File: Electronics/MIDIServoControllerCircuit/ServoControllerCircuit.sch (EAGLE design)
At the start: 19 parts, among them IC1 MCP1700INLINE, J1 PJ-063BH, T1 2N3904, X1 SIGNAL-PWR-GND, X2 SIGNAL-PWR-GND

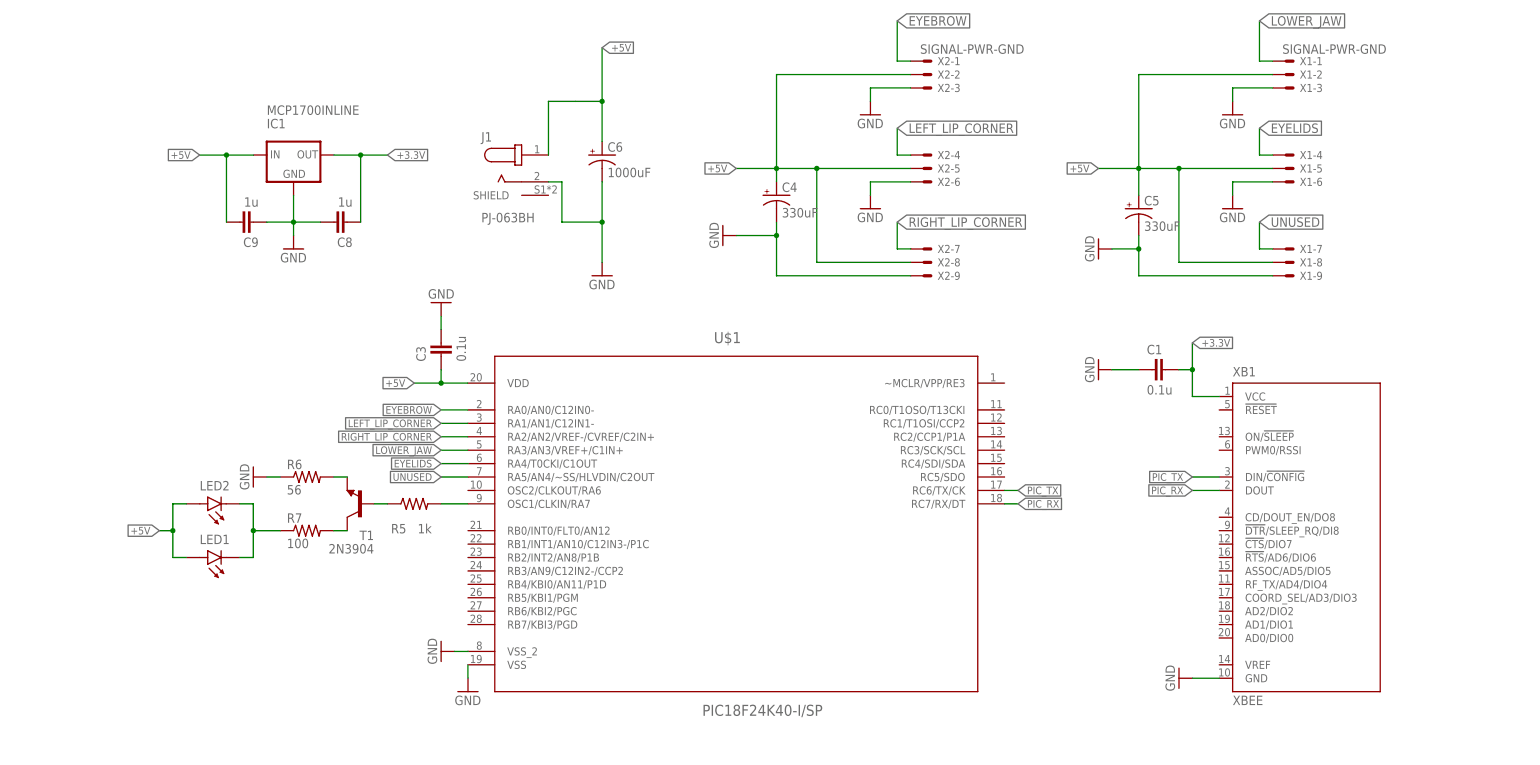
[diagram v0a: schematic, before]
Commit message: Reversing modifications made to Electronics that are ahread of the rest of the project.
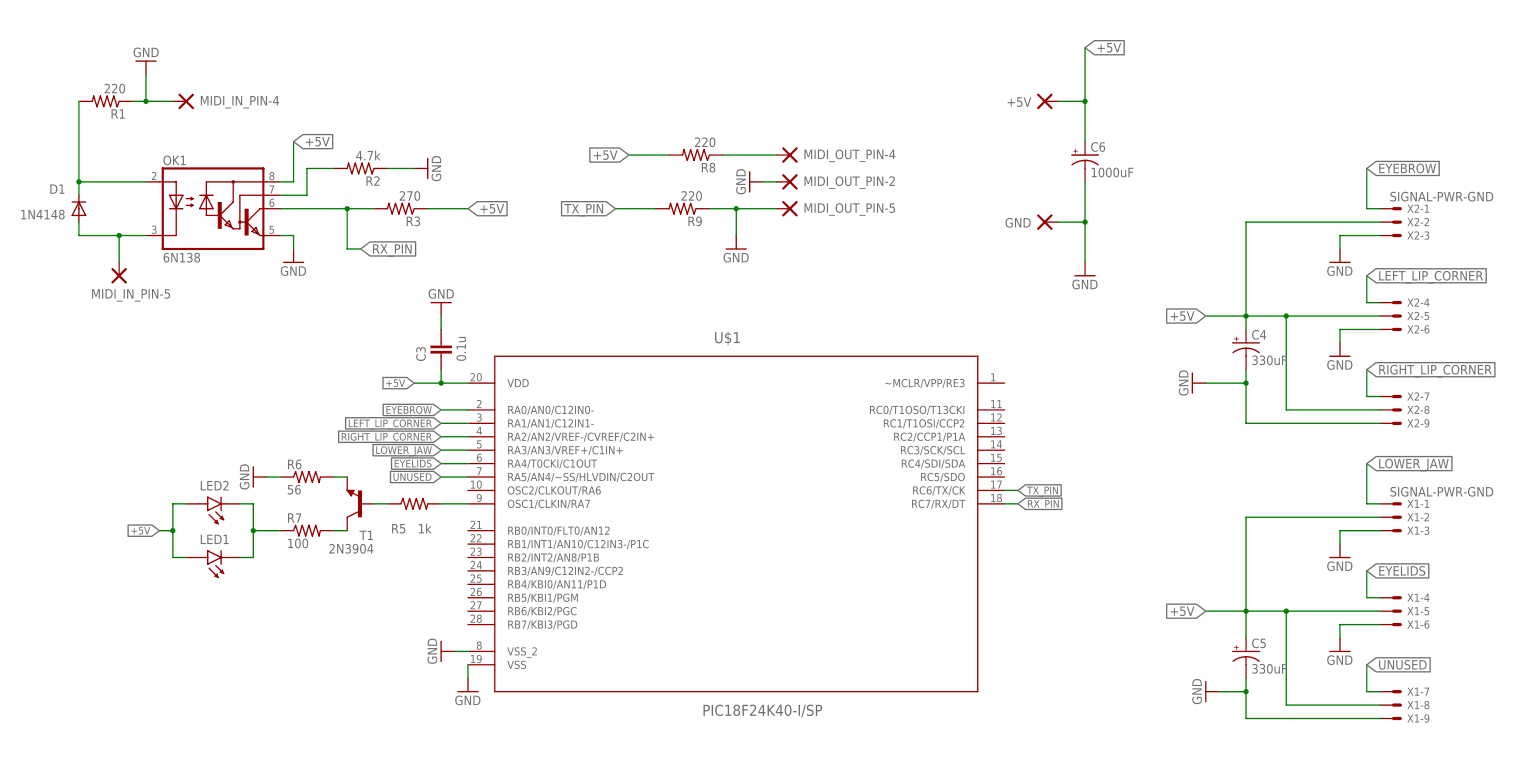
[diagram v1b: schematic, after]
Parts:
- removed C1: 0.1u, resistor:C-EU050-025X075
- removed C8, C9: 1u, resistor:C-EU050-025X075
- removed IC1: MCP1700INLINE, MCP1700:MCP1700INLINE
- removed J1: PJ-063BH, PJ-063BH:PJ-063BH
- removed XB1: XBEE, maxstream:XBEE
- added +5V, GND, MIDI_IN_PIN-4, MIDI_IN_PIN-5, MIDI_OUT_PIN-2, MIDI_OUT_PIN-4, MIDI_OUT_PIN-5: DOUBLE_THROUGH_HOLE_PAD, DOUBLE_THROUGH_HOLE_PAD:DOUBLE_THROUGH_HOLE_PAD
- added D1: 1N4148, diode:1N4148DO35-10
- added OK1: 6N138, optocoupler:6N138
- added R1, R8, R9: 220, resistor:R-US_0207/12
- added R2: 4.7k, resistor:R-US_0207/12
- added R3: 270, resistor:R-US_0207/12
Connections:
- removed net +3.3V: C1.1, C8.2, IC1.OUT, XB1.VCC
- removed net PIC_RX: U$1.RC7/RX/DT, XB1.DOUT
- removed net PIC_TX: U$1.RC6/TX/CK, XB1.DIN/!CONFIG
- new net MIDI_PIN-5: D1.A, MIDI_IN_PIN-5.P$1, OK1.C
- new net N$1: D1.C, OK1.A, R1.2
- new net N$11: MIDI_OUT_PIN-4.P$1, R8.1
- new net N$2: OK1.VB, R2.2
- new net RX_PIN: OK1.VO, R3.2, U$1.RC7/RX/DT
- new net TX_PIN: R9.2, U$1.RC6/TX/CK
- net +5V: now also +5V.P$1, OK1.VCC, R3.1, R8.2; no longer C9.1, IC1.IN, J1.1
- net GND: now also GND.P$1, MIDI_IN_PIN-4.P$1, MIDI_OUT_PIN-2.P$1, MIDI_OUT_PIN-5.P$1, OK1.GND, R1.1, R2.1, R9.1; no longer C1.2, C8.1, C9.2, IC1.GND, J1.2, XB1.GND
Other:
- moved on the sheet: C4, C5, C6, X1-1, X1-2, X1-3, X1-4, X1-5, X1-6, X1-7, X1-8, X1-9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

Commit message: Reversed modifications made to Electronics that are ahead of the rest of the project.
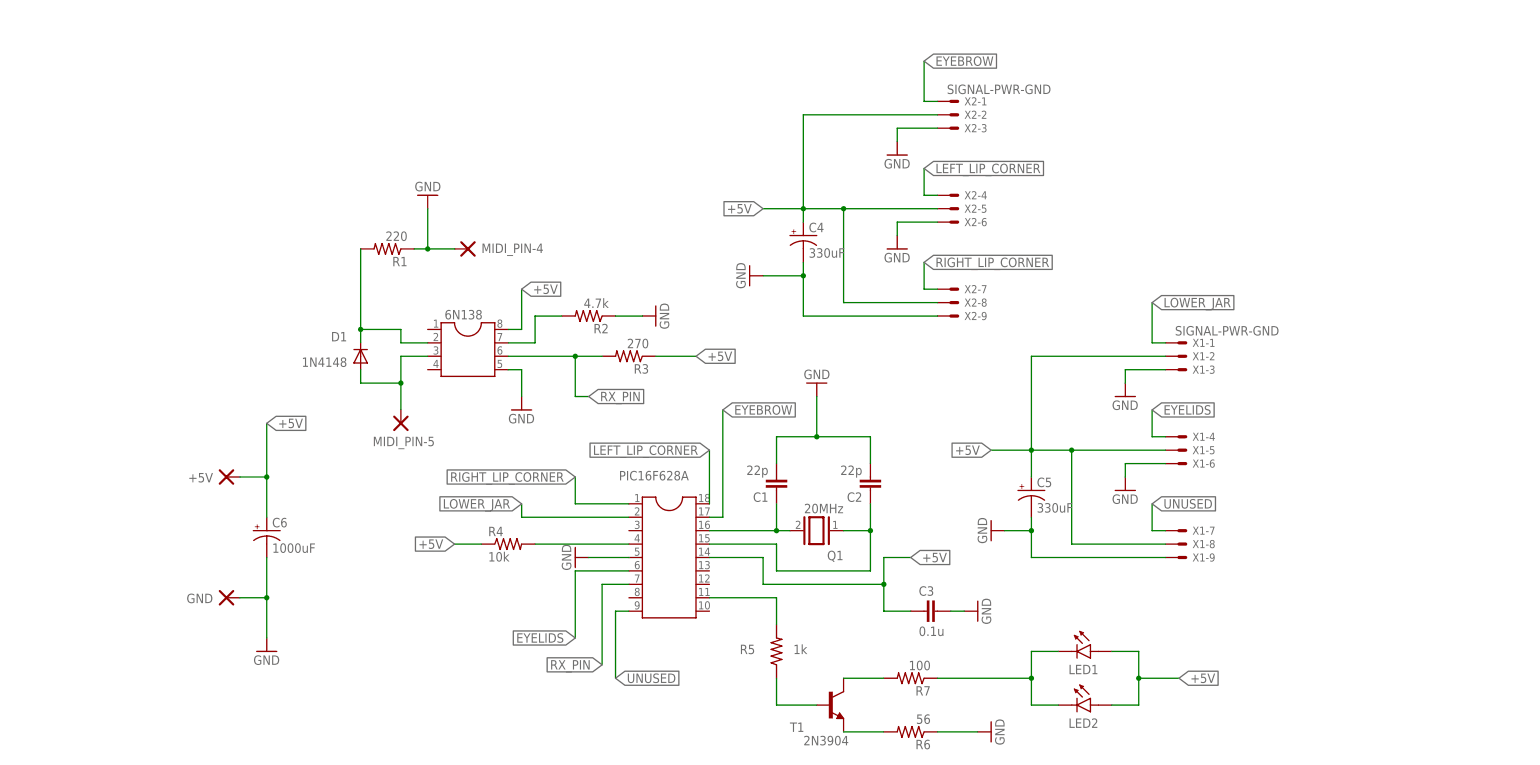
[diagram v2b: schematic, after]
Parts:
- removed MIDI_IN_PIN-4, MIDI_IN_PIN-5, MIDI_OUT_PIN-2, MIDI_OUT_PIN-4, MIDI_OUT_PIN-5: DOUBLE_THROUGH_HOLE_PAD, DOUBLE_THROUGH_HOLE_PAD:DOUBLE_THROUGH_HOLE_PAD
- removed OK1: 6N138, optocoupler:6N138
- removed R8, R9: 220, resistor:R-US_0207/12
- removed U$1: PIC18F24K40-I/SP, Microchip_By_element14_Batch_1:PIC18F24K20-I/SP
- added 6N138: (no value), ic-package:DIL8S
- added C1, C2: 22p, resistor:C-EU050-025X075
- added MIDI_PIN-4, MIDI_PIN-5: DOUBLE_THROUGH_HOLE_PAD, DOUBLE_THROUGH_HOLE_PAD:DOUBLE_THROUGH_HOLE_PAD
- added PIC16F628A: (no value), ic-package:DIL18S
- added Q1: 20MHz, special:XTAL/S
- added R4: 10k, resistor:R-US_0207/12
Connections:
- removed net LOWER_JAW: U$1.RA3/AN3/VREF+/C1IN+, X1-1.S
- removed net N$11: MIDI_OUT_PIN-4.P$1, R8.1
- removed net TX_PIN: R9.2, U$1.RC6/TX/CK
- new net LOWER_JAR: PIC16F628A.2, X1-1.S
- new net N$3: C1.1, PIC16F628A.16, Q1.2
- new net N$4: C2.1, PIC16F628A.15, Q1.1
- new net N$6: PIC16F628A.4, R4.2
- net +5V: now also 6N138.8, PIC16F628A.14, R4.1; no longer OK1.VCC, R8.2, U$1.VDD
- net EYEBROW: now also PIC16F628A.17; no longer U$1.RA0/AN0/C12IN0-
- net EYELIDS: now also PIC16F628A.6; no longer U$1.RA4/T0CKI/C1OUT
- net GND: now also 6N138.5, C1.2, C2.2, MIDI_PIN-4.P$1, PIC16F628A.5; no longer MIDI_IN_PIN-4.P$1, MIDI_OUT_PIN-2.P$1, MIDI_OUT_PIN-5.P$1, OK1.GND, R9.1, U$1.VSS, U$1.VSS_2
- net LEFT_LIP_CORNER: now also PIC16F628A.18; no longer U$1.RA1/AN1/C12IN1-
- net LIGHTS: now also PIC16F628A.11; no longer U$1.OSC1/CLKIN/RA7
- net MIDI_PIN-5: now also 6N138.3, MIDI_PIN-5.P$1; no longer MIDI_IN_PIN-5.P$1, OK1.C
- net N$1: now also 6N138.2; no longer OK1.A
- net N$2: now also 6N138.7; no longer OK1.VB
- net RIGHT_LIP_CORNER: now also PIC16F628A.1; no longer U$1.RA2/AN2/VREF-/CVREF/C2IN+
- net RX_PIN: now also 6N138.6, PIC16F628A.7; no longer OK1.VO, U$1.RC7/RX/DT
- net UNUSED: now also PIC16F628A.9; no longer U$1.RA5/AN4/~SS/HLVDIN/C2OUT
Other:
- moved on the sheet: +5V, C3, C4, C5, C6, D1, GND, LED1, LED2, R1, R2, R3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
